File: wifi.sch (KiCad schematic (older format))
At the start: 10 parts

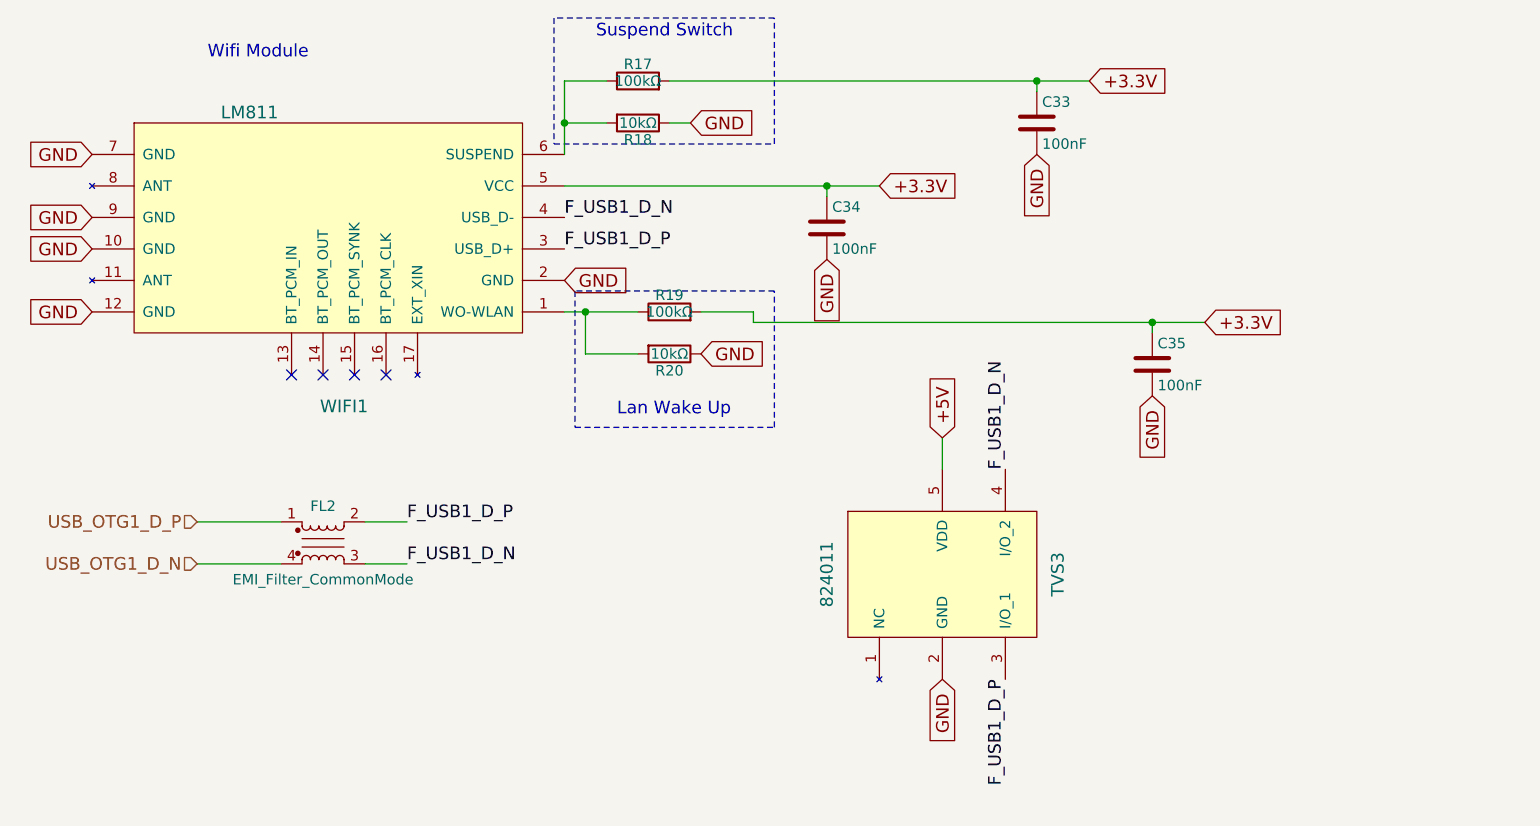
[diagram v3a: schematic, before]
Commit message: the components roughly spaced on the pcb
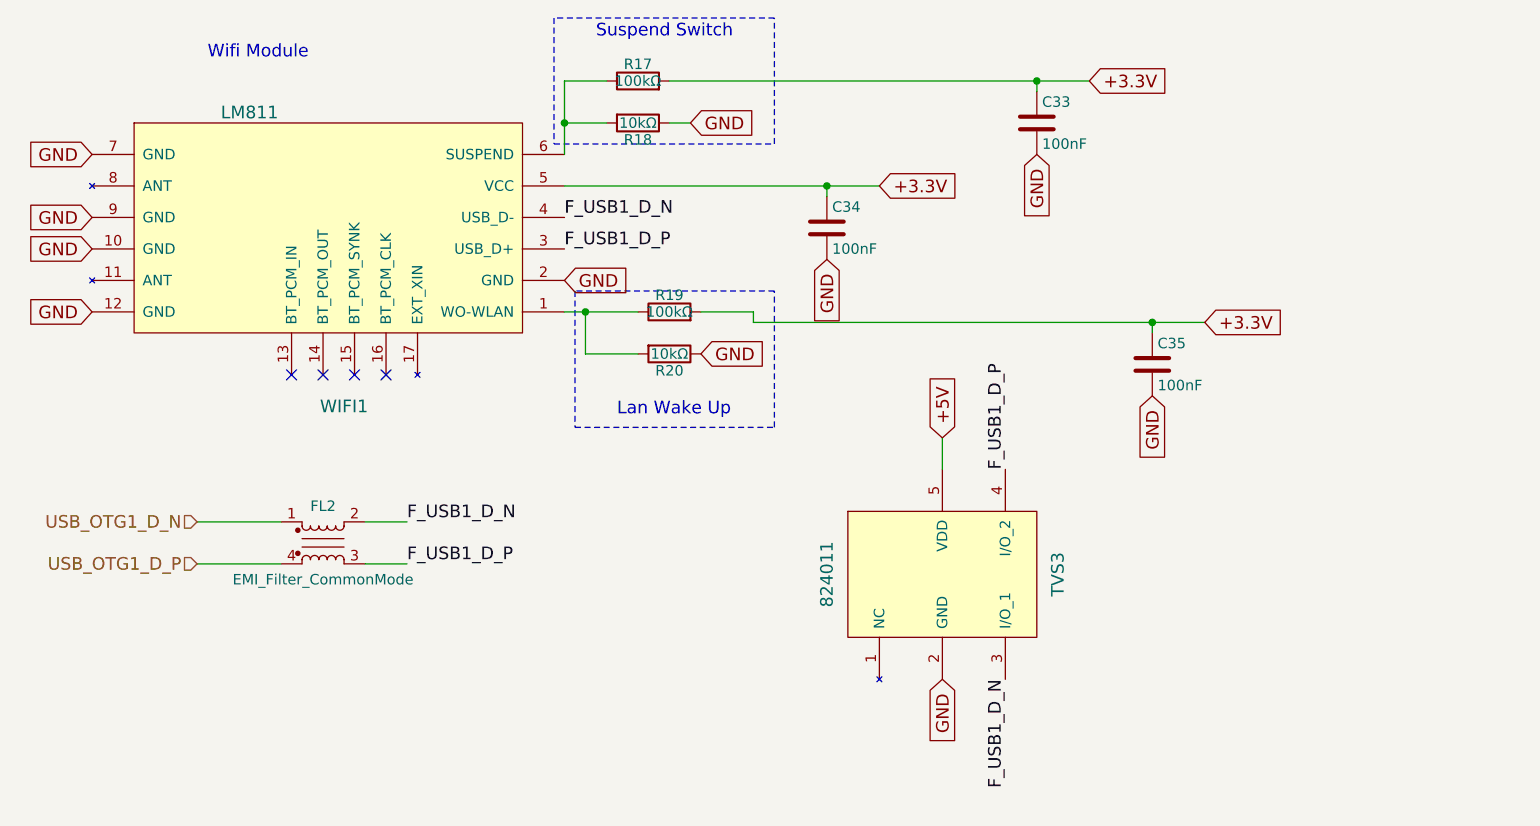
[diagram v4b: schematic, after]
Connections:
- net F_USB1_D_N: now also FL2.2, TVS3.3 (I/O_1); no longer FL2.3, TVS3.4 (I/O_2)
- net F_USB1_D_P: now also FL2.3, TVS3.4 (I/O_2); no longer FL2.2, TVS3.3 (I/O_1)
- net USB_OTG1_D_N: now also FL2.1; no longer FL2.4
- net USB_OTG1_D_P: now also FL2.4; no longer FL2.1
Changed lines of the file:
@@
 	1    0    0    -1
 $EndComp
+Text HLabel 1550 3200 0    60   Input ~ 0
+USB_OTG1_D_P
 Text HLabel 1550 3000 0    60   Input ~ 0
-USB_OTG1_D_P
-Text HLabel 1550 3200 0    60   Input ~ 0
 USB_OTG1_D_N
+Text Label 2550 3200 0    60   ~ 0
+F_USB1_D_P
 Text Label 2550 3000 0    60   ~ 0
-F_USB1_D_P
-Text Label 2550 3200 0    60   ~ 0
 F_USB1_D_N
 $Comp
@@
 Text Label 3300 1700 0    60   ~ 0
 F_USB1_D_P
+Text Label 5400 2750 1    60   ~ 0
+F_USB1_D_P
 Text Label 5400 3750 3    60   ~ 0
-F_USB1_D_P
-Text Label 5400 2750 1    60   ~ 0
 F_USB1_D_N
 Text GLabel 4800 1400 2    60   Input ~ 0

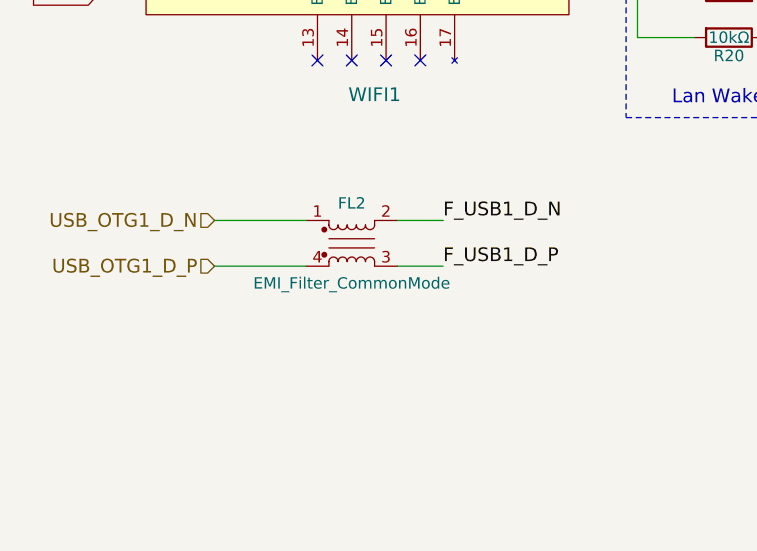
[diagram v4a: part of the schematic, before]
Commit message: almost completely routed; few missing routes
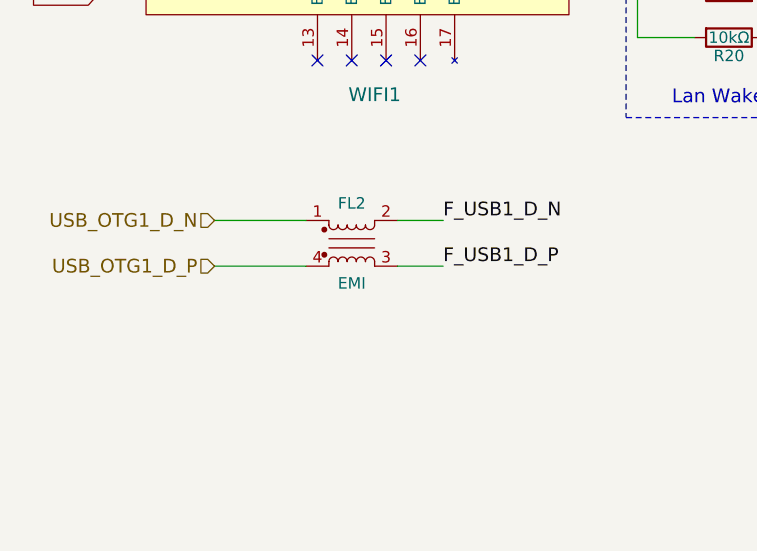
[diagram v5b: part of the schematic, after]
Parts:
- FL2: value EMI_Filter_CommonMode -> EMI
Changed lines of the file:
@@
 EESchema Schematic File Version 2
 LIBS:viztisztito-rescue
-LIBS:power
-LIBS:device
-LIBS:transistors
-LIBS:conn
-LIBS:linear
-LIBS:regul
-LIBS:74xx
-LIBS:cmos4000
-LIBS:adc-dac
-LIBS:memory
-LIBS:xilinx
-LIBS:microcontrollers
-LIBS:dsp
-LIBS:microchip
-LIBS:analog_switches
-LIBS:motorola
-LIBS:texas
-LIBS:intel
-LIBS:audio
-LIBS:interface
-LIBS:digital-audio
-LIBS:philips
-LIBS:display
-LIBS:cypress
-LIBS:siliconi
-LIBS:opto
-LIBS:atmel
-LIBS:contrib
-LIBS:valves
-LIBS:analog_devices
 LIBS:vtx-214-015-112
 LIBS:viztisztito-cache
@@
 LIBS:RFSolutions
 LIBS:switches
-EELAYER 25 0
+LIBS:74xgxx
+LIBS:74xx
+LIBS:ac-dc
+LIBS:actel
+LIBS:adc-dac
+LIBS:allegro
+LIBS:Altera
+LIBS:analog_devices
+LIBS:analog_switches
+LIBS:atmel
+LIBS:audio
+LIBS:battery_management
+LIBS:bbd
+LIBS:bosch
+LIBS:brooktre
+LIBS:cmos4000
+LIBS:conn
+LIBS:contrib
+LIBS:cypress
+LIBS:device
+LIBS:digital-audio
+LIBS:diode
+LIBS:display
+LIBS:dsp
+LIBS:elec-unifil
+LIBS:ESD_Protection
+LIBS:ftdi
+LIBS:gennum
+LIBS:graphic_symbols
+LIBS:hc11
+LIBS:infineon
+LIBS:intel
+LIBS:interface
+LIBS:intersil
+LIBS:ir
+LIBS:Lattice
+LIBS:leds
+LIBS:LEM
+LIBS:linear
+LIBS:logic_programmable
+LIBS:maxim
+LIBS:mechanical
+LIBS:memory
+LIBS:microchip
+LIBS:microchip_dspic33dsc
+LIBS:microchip_pic10mcu
+LIBS:microchip_pic12mcu
+LIBS:microchip_pic16mcu
+LIBS:microchip_pic18mcu
+LIBS:microchip_pic24mcu
+LIBS:microchip_pic32mcu
+LIBS:microcontrollers
+LIBS:modules
+LIBS:motor_drivers
+LIBS:motorola
+LIBS:motors
+LIBS:msp430
+LIBS:nordicsemi
+LIBS:nxp
+LIBS:nxp_armmcu
+LIBS:onsemi
+LIBS:opto
+LIBS:Oscillators
+LIBS:philips
+LIBS:power
+LIBS:powerint
+LIBS:Power_Management
+LIBS:pspice
+LIBS:references
+LIBS:regul
+LIBS:relays
+LIBS:rfcom
+LIBS:sensors
+LIBS:silabs
+LIBS:siliconi
+LIBS:stm8
+LIBS:stm32
+LIBS:supertex
+LIBS:texas
+LIBS:transf
+LIBS:transistors
+LIBS:triac_thyristor
+LIBS:ttl_ieee
+LIBS:valves
+LIBS:video
+LIBS:wiznet
+LIBS:Worldsemi
+LIBS:Xicor
+LIBS:xilinx
+LIBS:Zilog
+LIBS:crystals_oscillators
+LIBS:Diodes
+LIBS:discrete_transistors
+LIBS:microcontrollers_dspic33dsc
+LIBS:microcontrollers_msp430
+LIBS:microcontrollers_pic10mcu
+LIBS:microcontrollers_pic12mcu
+LIBS:microcontrollers_pic16mcu
+LIBS:microcontrollers_pic18mcu
+LIBS:microcontrollers_pic32mcu
+LIBS:microcontrollers_stm8
+LIBS:microcontrollers_stm32
+LIBS:microcontrollers_xmc
+LIBS:misc
+LIBS:Passives
+LIBS:regulators
+LIBS:rf
+EELAYER 26 0
 EELAYER END
 $Descr A4 11693 8268
@@
 P 2150 3100
 F 0 "FL2" H 2150 3275 50  0000 C CNN
-F 1 "EMI_Filter_CommonMode" H 2150 2925 50  0000 C CNN
+F 1 "EMI" H 2150 2925 50  0000 C CNN
 F 2 "water:744233121" V 2150 3140 50  0001 C CNN
 F 3 "http://hu.farnell.com/wurth-elektronik/744233121/line-filter-lvds-0805-120ohm-0/dp/1848957" V 2150 3140 50  0001 C CNN

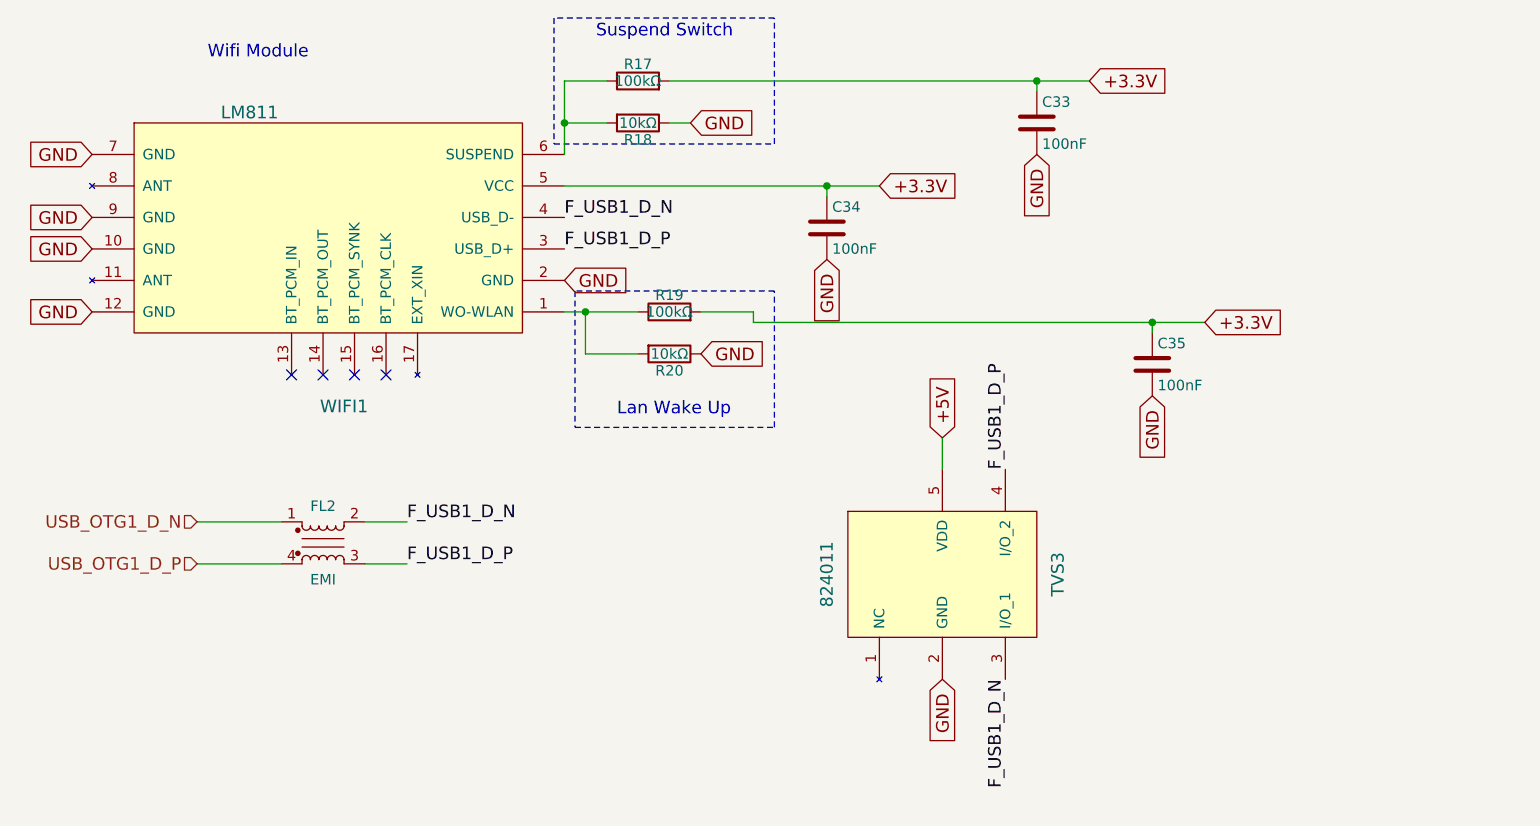
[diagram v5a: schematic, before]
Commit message: This version contains the final revision before the part footprint verification.
- The fuse is now moved outside of the power module before any parts
- The wifi module has an additional pair of 22R differential resistors
- The minor moves in the power power supply of the wifi module
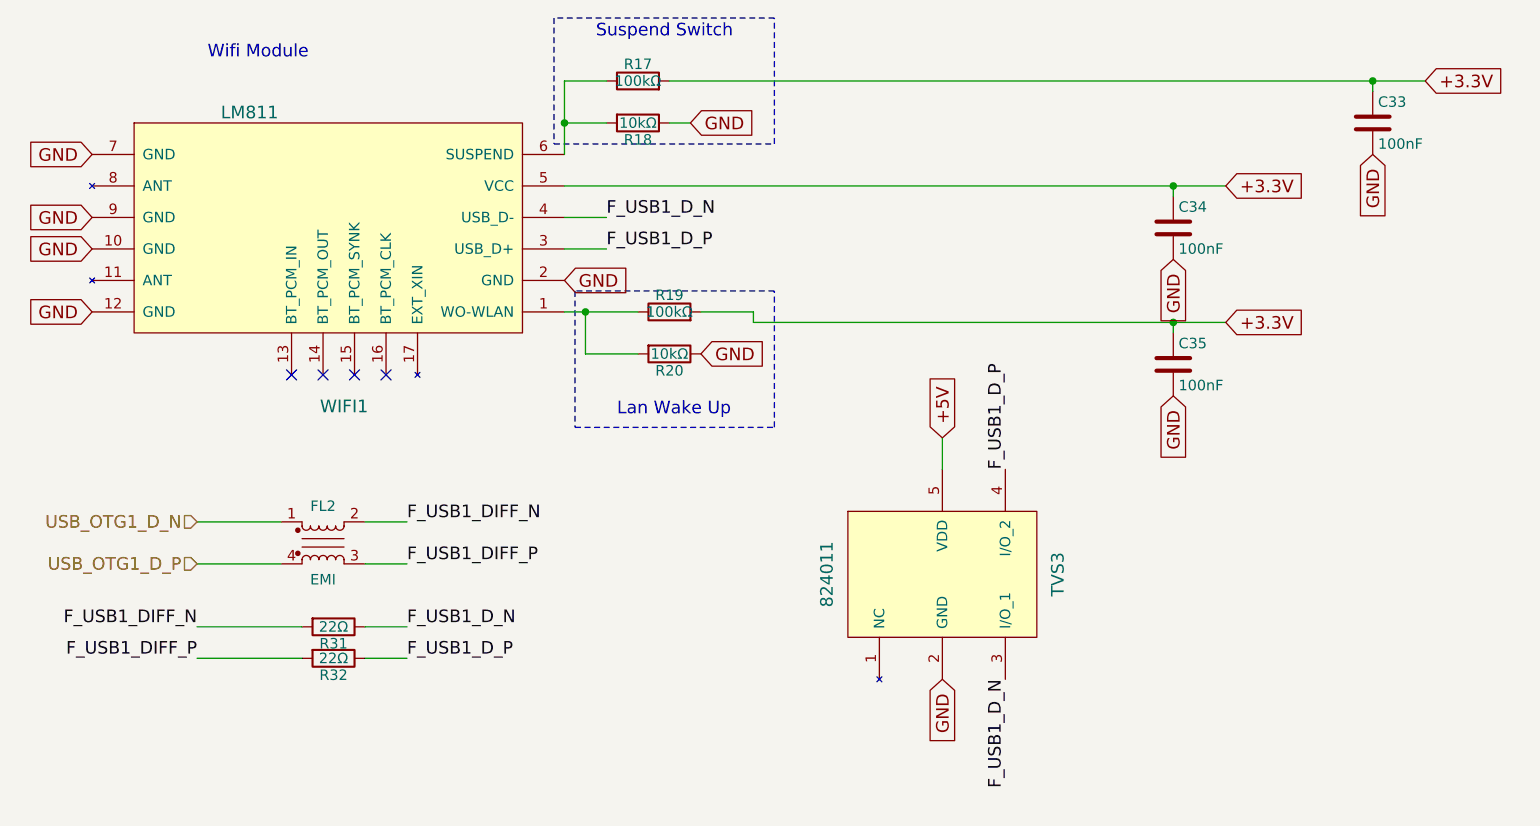
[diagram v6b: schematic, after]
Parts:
- added R31, R32: 22Ω, Resistors_SMD:R_0603_HandSoldering, symbol R
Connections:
- net F_USB1_D_N: now also R31.1; no longer FL2.2
- net F_USB1_D_P: now also R32.1; no longer FL2.3
- new net F_USB1_DIFF_N: FL2.2, R31.2
- new net F_USB1_DIFF_P: FL2.3, R32.2
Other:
- moved on the sheet: C33, C34, C35
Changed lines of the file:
@@
 Text HLabel 1550 3000 0    60   Input ~ 0
 USB_OTG1_D_N
-Text Label 2550 3200 0    60   ~ 0
-F_USB1_D_P
-Text Label 2550 3000 0    60   ~ 0
-F_USB1_D_N
 $Comp
 L 824011 TVS3
@@
 Text GLabel 5100 3750 3    60   Input ~ 0
 GND
-Text Label 3300 1550 0    60   ~ 0
+Text Label 2550 3500 0    60   ~ 0
 F_USB1_D_N
-Text Label 3300 1700 0    60   ~ 0
+Text Label 2550 3650 0    60   ~ 0
 F_USB1_D_P
 Text Label 5400 2750 1    60   ~ 0
@@
 Text Label 5400 3750 3    60   ~ 0
 F_USB1_D_N
-Text GLabel 4800 1400 2    60   Input ~ 0
+Text GLabel 6450 1400 2    60   Input ~ 0
 +3.3V
-Text GLabel 4550 1750 3    60   Input ~ 0
+Text GLabel 6200 1750 3    60   Input ~ 0
 GND
 Wire Wire Line
@@
 	3800 1100 3900 1100
 Wire Wire Line
-	3800 900  5800 900
+	3800 900  7400 900
 Wire Wire Line
 	1550 3000 1950 3000
@@
 	2350 3200 2550 3200
 Wire Wire Line
-	4800 1400 3300 1400
-Wire Wire Line
-	4550 1450 4550 1400
-Connection ~ 4550 1400
+	3300 1400 6450 1400
+Wire Wire Line
+	6200 1450 6200 1400
+Connection ~ 6200 1400
 Wire Notes Line
 	3350 2550 4300 2550
@@
 L C C34
 U 1 1 59A67E6E
-P 4550 1600
-F 0 "C34" H 4575 1700 50  0000 L CNN
-F 1 "100nF" H 4575 1500 50  0000 L CNN
-F 2 "Capacitors_SMD:C_0603_HandSoldering" H 4588 1450 30  0001 C CNN
-F 3 "hu.farnell.com/avx/06035c104kat2a/cap-mlcc-x7r-100nf-50v-0603/dp/1301804" H 4550 1600 60  0001 C CNN
-	1    4550 1600
+P 6200 1600
+F 0 "C34" H 6225 1700 50  0000 L CNN
+F 1 "100nF" H 6225 1500 50  0000 L CNN
+F 2 "Capacitors_SMD:C_0603_HandSoldering" H 6238 1450 30  0001 C CNN
+F 3 "hu.farnell.com/avx/06035c104kat2a/cap-mlcc-x7r-100nf-50v-0603/dp/1301804" H 6200 1600 60  0001 C CNN
+	1    6200 1600
 	1    0    0    -1
 $EndComp
@@
 	0    1    1    0
 $EndComp
-Text GLabel 5800 900  2    60   Input ~ 0
+Text GLabel 7400 900  2    60   Input ~ 0
 +3.3V
-Text GLabel 5550 1250 3    60   Input ~ 0
-GND
-Wire Wire Line
-	5550 950  5550 900
-Connection ~ 5550 900
+Text GLabel 7150 1250 3    60   Input ~ 0
+GND
+Wire Wire Line
+	7150 950  7150 900
+Connection ~ 7150 900
 $Comp
 L C C33
 U 1 1 59AA68FC
-P 5550 1100
-F 0 "C33" H 5575 1200 50  0000 L CNN
-F 1 "100nF" H 5575 1000 50  0000 L CNN
-F 2 "Capacitors_SMD:C_0603_HandSoldering" H 5588 950 30  0001 C CNN
-F 3 "hu.farnell.com/avx/06035c104kat2a/cap-mlcc-x7r-100nf-50v-0603/dp/1301804" H 5550 1100 60  0001 C CNN
-	1    5550 1100
-	1    0    0    -1
-$EndComp
-Wire Wire Line
-	4200 2050 6350 2050
-Text GLabel 6350 2050 2    60   Input ~ 0
+P 7150 1100
+F 0 "C33" H 7175 1200 50  0000 L CNN
+F 1 "100nF" H 7175 1000 50  0000 L CNN
+F 2 "Capacitors_SMD:C_0603_HandSoldering" H 7188 950 30  0001 C CNN
+F 3 "hu.farnell.com/avx/06035c104kat2a/cap-mlcc-x7r-100nf-50v-0603/dp/1301804" H 7150 1100 60  0001 C CNN
+	1    7150 1100
+	1    0    0    -1
+$EndComp
+Wire Wire Line
+	4200 2050 6450 2050
+Text GLabel 6450 2050 2    60   Input ~ 0
 +3.3V
-Text GLabel 6100 2400 3    60   Input ~ 0
-GND
-Wire Wire Line
-	6100 2100 6100 2050
-Connection ~ 6100 2050
+Text GLabel 6200 2400 3    60   Input ~ 0
+GND
+Wire Wire Line
+	6200 2100 6200 2050
+Connection ~ 6200 2050
 $Comp
 L C C35
 U 1 1 59AA69A3
-P 6100 2250
-F 0 "C35" H 6125 2350 50  0000 L CNN
-F 1 "100nF" H 6125 2150 50  0000 L CNN
-F 2 "Capacitors_SMD:C_0603_HandSoldering" H 6138 2100 30  0001 C CNN
-F 3 "hu.farnell.com/avx/06035c104kat2a/cap-mlcc-x7r-100nf-50v-0603/dp/1301804" H 6100 2250 60  0001 C CNN
-	1    6100 2250
+P 6200 2250
+F 0 "C35" H 6225 2350 50  0000 L CNN
+F 1 "100nF" H 6225 2150 50  0000 L CNN
+F 2 "Capacitors_SMD:C_0603_HandSoldering" H 6238 2100 30  0001 C CNN
+F 3 "hu.farnell.com/avx/06035c104kat2a/cap-mlcc-x7r-100nf-50v-0603/dp/1301804" H 6200 2250 60  0001 C CNN
+	1    6200 2250
 	1    0    0    -1
 $EndComp
@@
 NoConn ~ 2300 2300
 NoConn ~ 2450 2300
+$Comp
+L R R31
+U 1 1 59B1CA73
+P 2200 3500
+F 0 "R31" V 2280 3500 50  0000 C CNN
+F 1 "22Ω" V 2200 3500 50  0000 C CNN
+F 2 "Resistors_SMD:R_0603_HandSoldering" V 2130 3500 50  0001 C CNN
+F 3 "http://hu.farnell.com/multicomp/mcwr06x22r0ftl/res-thick-film-22ohm-1-0-1w/dp/2447301" H 2200 3500 50  0001 C CNN
+	1    2200 3500
+	0    1    1    0
+$EndComp
+$Comp
+L R R32
+U 1 1 59B1CA7A
+P 2200 3650
+F 0 "R32" V 2280 3650 50  0000 C CNN
+F 1 "22Ω" V 2200 3650 50  0000 C CNN
+F 2 "Resistors_SMD:R_0603_HandSoldering" V 2130 3650 50  0001 C CNN
+F 3 "http://hu.farnell.com/multicomp/mcwr06x22r0ftl/res-thick-film-22ohm-1-0-1w/dp/2447301" H 2200 3650 50  0001 C CNN
+	1    2200 3650
+	0    1    1    0
+$EndComp
+Wire Wire Line
+	3300 1550 3500 1550
+Wire Wire Line
+	3300 1700 3500 1700
+Wire Wire Line
+	2350 3500 2550 3500
+Wire Wire Line
+	2350 3650 2550 3650
+Text Label 1550 3500 2    60   ~ 0
+F_USB1_DIFF_N
+Text Label 1550 3650 2    60   ~ 0
+F_USB1_DIFF_P
+Wire Wire Line
+	1550 3500 2050 3500
+Wire Wire Line
+	2050 3650 1550 3650
+Text Label 2550 3000 0    60   ~ 0
+F_USB1_DIFF_N
+Text Label 2550 3200 0    60   ~ 0
+F_USB1_DIFF_P
+Text Label 3500 1550 0    60   ~ 0
+F_USB1_D_N
+Text Label 3500 1700 0    60   ~ 0
+F_USB1_D_P
 $EndSCHEMATC
